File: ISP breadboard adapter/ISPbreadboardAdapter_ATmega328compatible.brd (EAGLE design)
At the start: 12.7 x 15.2 mm, 4 parts

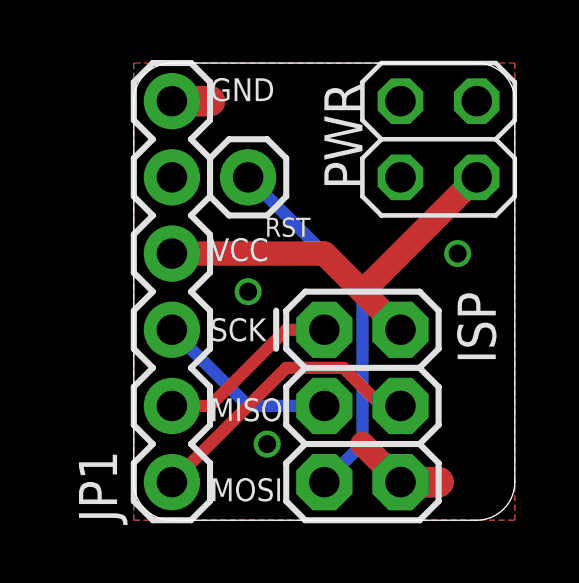
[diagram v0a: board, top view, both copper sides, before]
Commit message: added some info to silk screen
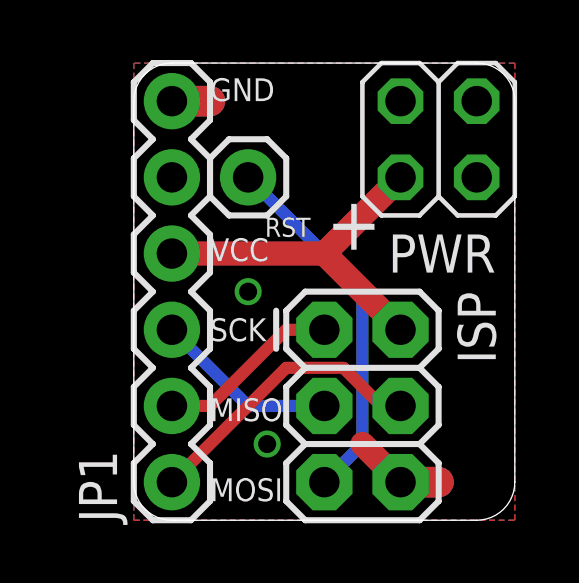
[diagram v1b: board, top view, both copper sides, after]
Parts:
- turned PWR to 180 degrees
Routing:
- net VCC: track 14.1 -> 12.3 mm
- net GND: vias 3 -> 2
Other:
- board text added: "+"
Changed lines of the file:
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@@
 <?xml version="1.0" encoding="utf-8"?>
 <!DOCTYPE eagle SYSTEM "eagle.dtd">
-<eagle version="6.6.0">
+<eagle version="7.3.0">
 <drawing>
 <settings>
@@
 <layer number="56" name="wert" color="7" fill="1" visible="no" active="no"/>
 <layer number="57" name="tCAD" color="7" fill="1" visible="no" active="no"/>
-<layer number="90" name="Modules" color="5" fill="1" visible="yes" active="yes"/>
+<layer number="90" name="Modules" color="5" fill="1" visible="no" active="no"/>
 <layer number="91" name="Nets" color="2" fill="1" visible="no" active="no"/>
 <layer number="92" name="Busses" color="1" fill="1" visible="no" active="no"/>
@@
 MISO
 MOSI</text>
+<text x="8.255" y="10.795" size="1.778" layer="25" rot="R180">+</text>
 </plain>
 <attributes>
@@
 <pass name="Default">
 <param name="RoutingGrid" value="50mil"/>
+<param name="AutoGrid" value="1"/>
+<param name="Efforts" value="0"/>
+<param name="TopRouterVariant" value="1"/>
 <param name="tpViaShape" value="round"/>
 <param name="PrefDir.1" value="|"/>
@@
 </autorouter>
 <elements>
-<element name="PWR" library="pinhead" package="2X02" value="" x="10.16" y="12.7" smashed="yes" rot="R270">
-<attribute name="NAME" x="6.35" y="14.605" size="1.27" layer="25" ratio="10" rot="R270"/>
-<attribute name="VALUE" x="5.715" y="15.24" size="1.27" layer="27" rot="R270"/>
+<element name="PWR" library="pinhead" package="2X02" value="" x="10.16" y="12.7" smashed="yes" rot="R180">
+<attribute name="NAME" x="12.065" y="9.525" size="1.27" layer="25" ratio="10" rot="R180"/>
+<attribute name="VALUE" x="12.7" y="17.145" size="1.27" layer="27" rot="R180"/>
 </element>
 <element name="RST" library="SparkFun-Connectors" package="1X01" value="" x="3.81" y="11.43" smashed="yes">
@@
 <contactref element="PWR" pad="4"/>
 <wire x1="1.27" y1="8.89" x2="6.35" y2="8.89" width="0.8128" layer="1"/>
-<wire x1="6.35" y1="8.89" x2="7.62" y2="7.62" width="0.8128" layer="1"/>
-<wire x1="7.62" y1="7.62" x2="8.89" y2="6.35" width="0.8128" layer="1"/>
-<wire x1="11.43" y1="11.43" x2="7.62" y2="7.62" width="0.8128" layer="1"/>
+<wire x1="6.35" y1="8.89" x2="8.89" y2="6.35" width="0.8128" layer="1"/>
+<wire x1="6.35" y1="8.89" x2="8.89" y2="11.43" width="0.8128" layer="1"/>
 </signal>
 <signal name="GND">
@@
 <via x="4.445" y="2.54" extent="1-16" drill="0.6"/>
 <wire x1="8.89" y1="1.27" x2="7.62" y2="2.54" width="0.8128" layer="1"/>
-<via x="10.795" y="8.89" extent="1-16" drill="0.6"/>
 </signal>
 <signal name="RST">

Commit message: updated .brd
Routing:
- net GND: vias 2 -> 6
